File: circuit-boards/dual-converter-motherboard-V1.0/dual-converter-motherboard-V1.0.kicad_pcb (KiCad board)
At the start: 6 copper layers, 230 x 76 mm, 107 parts, among them J1 2601-1102, J10 Conn_02x03_Odd_Even, J11 Conn_01x06_Socket, J12 Conn_02x03_Odd_Even, J13 Conn_02x03_Odd_Even, J14 Conn_02x03_Odd_Even, J15 Conn_01x06_Socket, J16 Conn_01x07_Socket, J2 2601-1102, J3 S4B-XH-SM4-TB, J4 Conn_02x03_Odd_Even, J5 Conn_02x03_Odd_Even, J6 Conn_02x03_Odd_Even, J7 Conn_02x03_Odd_Even, J8 Conn_02x03_Odd_Even, J9 Conn_02x03_Odd_Even, Q1 SUM110P08-11L-E3, Q2 DMP45H4D9HK3-13, Q3 SIHB068N60EF-GE3, U4 UCC23313BDWYR, U5 TMCS1133C1A, U6 UCC23313BDWYR, U7 UCC23313BDWYR, U8 SC0915

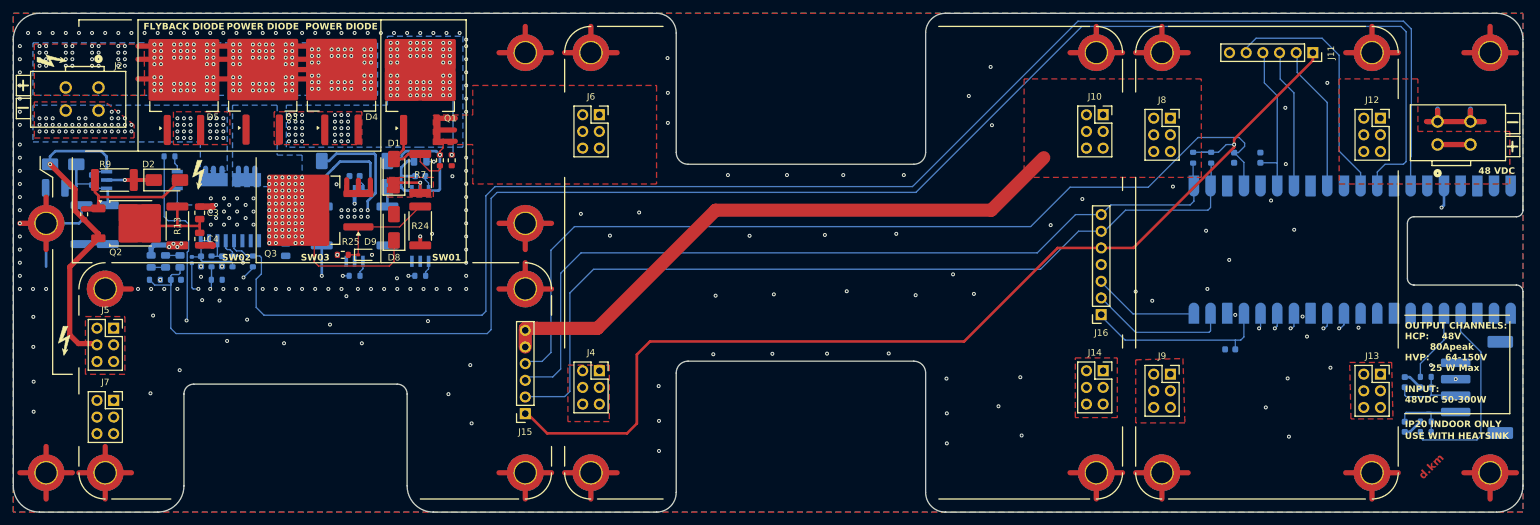
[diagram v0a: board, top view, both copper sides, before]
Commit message: fix edgecut interference with trace
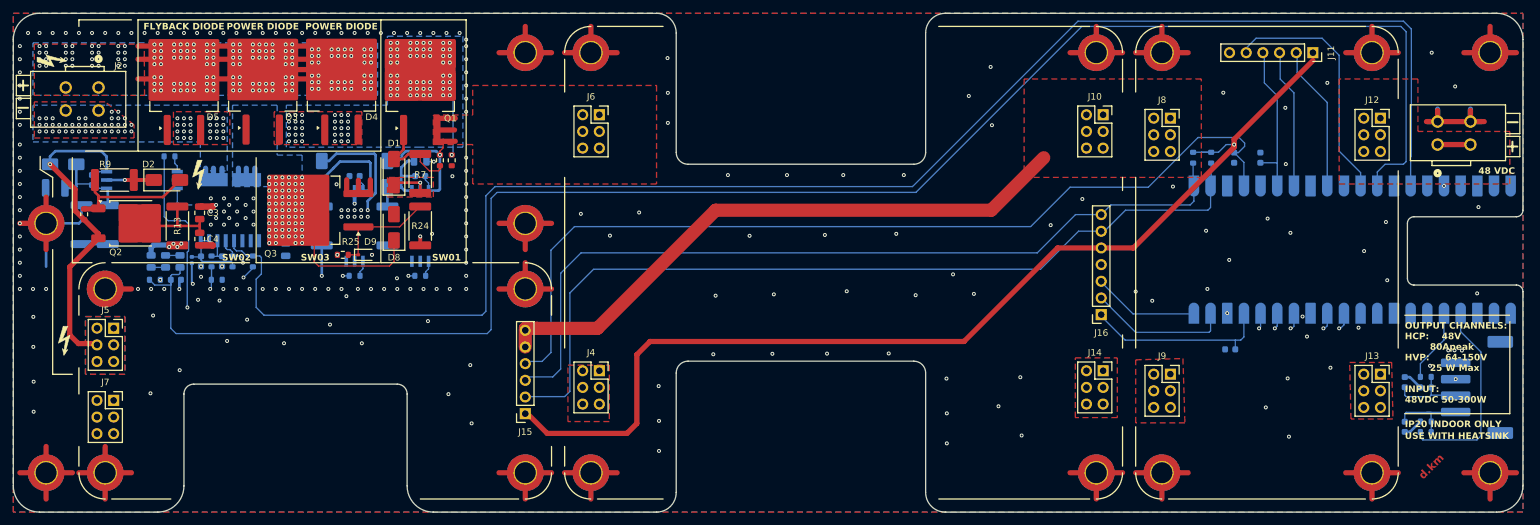
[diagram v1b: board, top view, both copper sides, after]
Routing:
- net +3.3V: track 323.5 -> 327.4 mm
- net /controller/SW_HIGH-VOLTAGE-PHASE: track 213.4 -> 211.3 mm
- net GND: track 297.2 -> 298.7 mm, vias 211 -> 222
- added copper zone on B.Cu, net /BOOST-CONVERTER-OUTPUT
- added copper zone on In1.Cu, net /BOOST-CONVERTER-OUTPUT
- added copper zone on In2.Cu, net /BOOST-CONVERTER-OUTPUT
- added copper zone on In3.Cu, net /BOOST-CONVERTER-OUTPUT
- added copper zone on In4.Cu, net /BOOST-CONVERTER-OUTPUT
